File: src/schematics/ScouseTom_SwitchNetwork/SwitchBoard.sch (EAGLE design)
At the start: 87 parts, among them T1 PNP, U1 MCP73831, U10 ADG714BRUZ, U11 ADG714BRUZ, U12 ADUM1410ARWZ, U13 ADG714BRUZ, U14 ADG714BRUZ, U15 ADUM1412ARWZ, U2 ADG714BRUZ, U3 ADG714BRUZ, U4 TPS61090RSAR, U5 ADG714BRUZ, U6 ADG714BRUZ, U7 ADG714BRUZ, U8 LT1763CDE-5, U9 ADG714BRUZ, X1 USB-MICROB, X2 CTR_ARD, X3 CTR_OUT, X4 DSUB _T, X5 DSUB_B, X6 CTR_IN

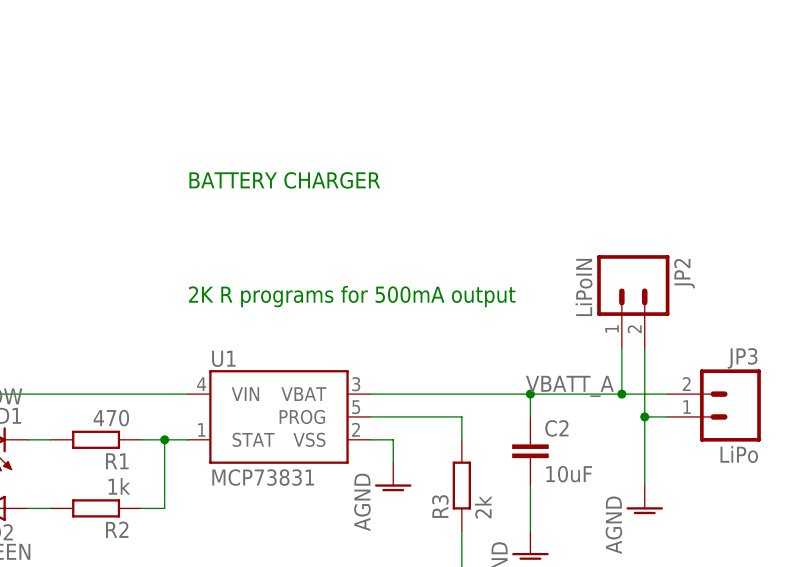
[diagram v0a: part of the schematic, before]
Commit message: Minor clarification in text in shcematic
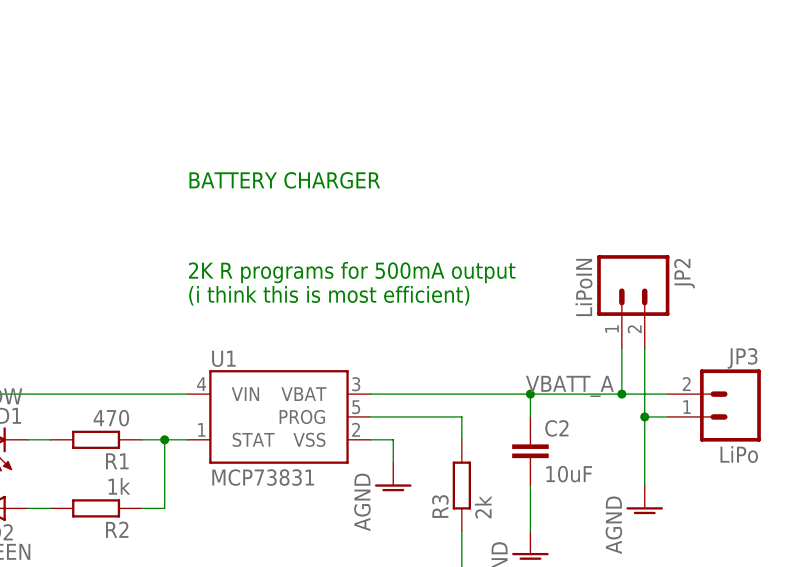
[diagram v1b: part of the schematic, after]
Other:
- note added: "2K R programs for 500mA output (i think this is most efficient)"
- note removed: "2K R programs for 500mA output"
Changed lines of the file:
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@@
 Split into free components</text>
 <text x="-246.38" y="208.28" size="1.778" layer="91">NOT CHANGED THIS YET</text>
-<text x="-490.22" y="203.2" size="1.778" layer="91">2K R programs for 500mA output</text>
+<text x="-490.22" y="203.2" size="1.778" layer="91">2K R programs for 500mA output
+(i think this is most efficient)</text>
 <text x="-416.56" y="220.98" size="1.778" layer="91">DISCONNECT BATTERY FROM REGULATORS TO TURN SHIT OFF</text>
 </plain>

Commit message: updated switchboard with proper daisy chain select and test 1 correct wiring
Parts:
- removed JP7: DCHN, pinhead:PINHD-2X9
- added U$1: PINHD-3X7GAP, pinhead:PINHD-3X7GAP
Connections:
- removed net GND_DCHN: JP7.4, X6.6
- removed net RESET_DCHN: JP7.14, X6.8
- removed net SYNC_DCHN: JP7.6, X6.4
- removed net TEST_1: JP7.15, R23.2, U15.VIC, X3.5
- removed net TEST_1_DCHN: JP7.16, X6.5
- new net DIN+_BRD: U$1.5, U12.VOB
- new net DIN-_BRD: U$1.7, U12.VOC
- new net SCLK_BRD: U$1.9, U12.VOD
- new net TEST_2_BRD: U$1.13, U15.VID
- new net VDD_BRD: C15.+, C18.1, C19.1, C24.1, C25.1, R23.2, U$1.1, U12.VDD2, U15.VDD2, U15.VIC, U8.OUT@1
- new net ~RESET_BRD: U$1.11, U15.VOA
- new net ~RESET_DCHN: U$1.12, X6.8
- new net ~SYNC_BRD: U$1.3, U12.VOA
- new net ~SYNC_DCHN: U$1.4, X6.4
- net AGND: now also X6.6; no longer JP7.3
- net DIN+: now also U$1.17; no longer JP7.7, U12.VOB
- net DIN+_DCHN: now also U$1.6; no longer JP7.8
- net DIN-: now also U$1.18; no longer JP7.9, U12.VOC
- net DIN-_DCHN: now also U$1.8; no longer JP7.10
- net SCLK: now also U$1.19; no longer JP7.11, U12.VOD
- net SCLK_DCHN: now also U$1.10; no longer JP7.12
- net TEST_2: now also U$1.21; no longer JP7.17, U15.VID
- net TEST_2_DCHN: now also U$1.14; no longer JP7.18
- net VDD: now also U$1.15, X3.5; no longer C15.+, C18.1, C19.1, C24.1, C25.1, JP7.1, U12.VDD2, U15.VDD2, U8.OUT@1
- net VDD_DCHN: now also U$1.2, X6.5; no longer JP7.2
- net ~RESET: now also U$1.20; no longer JP7.13, U15.VOA
- net ~SYNC: now also U$1.16; no longer JP7.5, U12.VOA

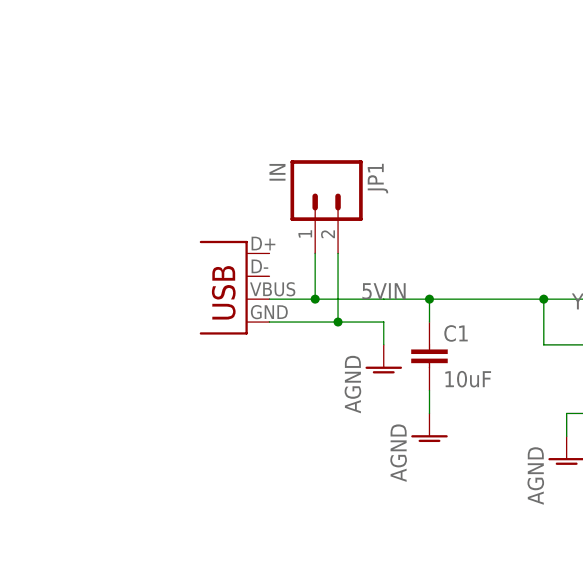
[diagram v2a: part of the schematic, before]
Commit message: Changed USB connector on SwitchBoard
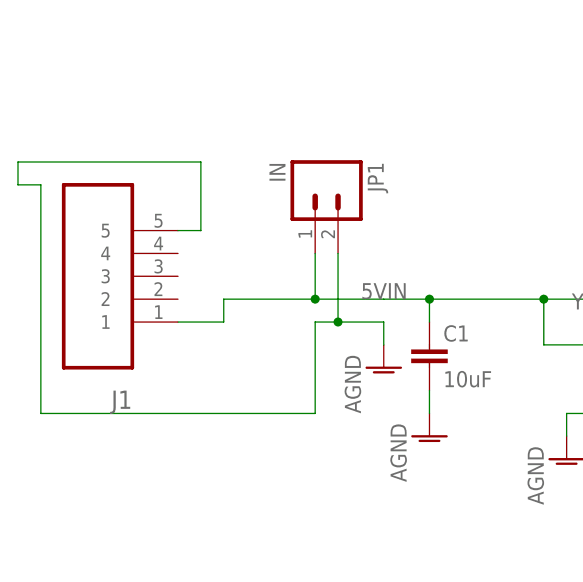
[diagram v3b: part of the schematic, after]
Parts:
- removed X1: USB-MICROB, SparkFun:USB-MICROB
- added J1: (no value), Molex-47346-0001:47346-0001
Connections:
- net 5VIN: now also J1.1; no longer X1.VBUS
- net AGND: now also J1.5; no longer X1.GND

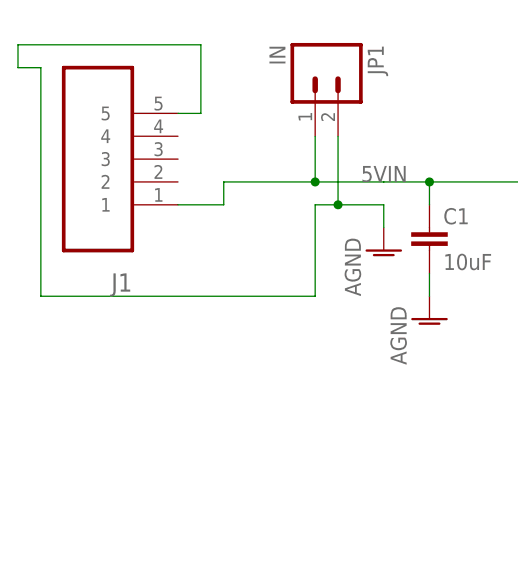
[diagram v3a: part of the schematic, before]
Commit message: Minor Silkscreen updates to SwitchBoard. New Gerber files and updated BOM and P&P with lipo connector
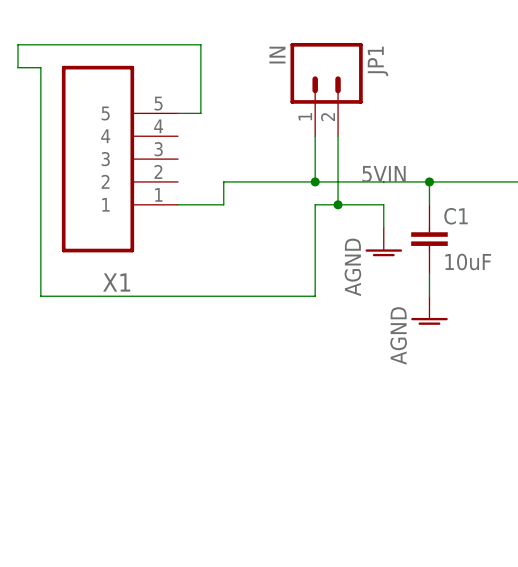
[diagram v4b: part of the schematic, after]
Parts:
- renumbered J1 to X1
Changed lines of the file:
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@@
 <part name="AGND51" library="supply1" deviceset="AGND" device=""/>
 <part name="U$1" library="pinhead" deviceset="PINHD-3X7GAP" device=""/>
-<part name="J1" library="Molex-47346-0001" deviceset="47346-0001" device=""/>
+<part name="X1" library="Molex-47346-0001" deviceset="47346-0001" device=""/>
 </parts>
 <sheets>
@@
 <instance part="AGND51" gate="VR1" x="248.92" y="121.92" rot="R90"/>
 <instance part="U$1" gate="G$1" x="383.54" y="114.3"/>
-<instance part="J1" gate="G$1" x="-571.5" y="195.58" rot="R180"/>
+<instance part="X1" gate="G$1" x="-571.5" y="195.58" rot="R180"/>
 </instances>
 <busses>
@@
 <pinref part="JP1" gate="G$1" pin="2"/>
 <pinref part="AGND1" gate="VR1" pin="AGND"/>
-<pinref part="J1" gate="G$1" pin="5"/>
+<pinref part="X1" gate="G$1" pin="5"/>
 <wire x1="-561.34" y1="200.66" x2="-558.8" y2="200.66" width="0.1524" layer="91"/>
 <wire x1="-558.8" y1="200.66" x2="-558.8" y2="208.28" width="0.1524" layer="91"/>
@@
 <wire x1="-556.26" y1="193.04" x2="-556.26" y2="190.5" width="0.1524" layer="91"/>
 <junction x="-546.1" y="193.04"/>
-<pinref part="J1" gate="G$1" pin="1"/>
+<pinref part="X1" gate="G$1" pin="1"/>
 <wire x1="-556.26" y1="190.5" x2="-561.34" y2="190.5" width="0.1524" layer="91"/>
 </segment>

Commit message: Updated Switchboard - pull down resistors, fixed routing, protection diodes and different battery connector
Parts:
- removed JP2: LiPoIN, SparkFun:M02PTH
- removed JP3: LiPo, SparkFun:M02-JST-2MM-SMT
- added D1, D2: 1N4148W-7-F, diode:DIODE-SOD123
- added R25, R26, R27, R28, R29, R30, R31, R32, R33, R34, R35, R36, R37, R38: 10k, rcl:R-EU_R0402
- added TP1, TP2: TPPAD1-20, testpad:TPPAD1-20
- added X7: JST-XH-02-PIN-LONG-PAD, Rembrandt Electronics - JST XH Connectors v1-0:JST-XH-02-PIN-LONG-PAD
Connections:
- net N$12 renamed CTR_IN_SHLD
- net 5VIN: now also D1.C
- net AGND: now also D1.A, D2.A, R30.1, R33.1, R34.1, R35.1, R36.1, R37.1, R38.1, X7-1.S; no longer JP2.2, JP3.1
- net DIN+_DCHN: now also R36.2
- net DIN+_IN: now also R29.2
- net DIN-_DCHN: now also R37.2
- net DIN-_IN: now also R32.2
- net GND: now also R25.2, R26.2, R27.1, R28.1, R29.1, R31.1, R32.1
- net IN+: now also TP1.TP
- net IN-: now also TP2.TP
- net RESET_IN: now also R31.2
- net SCLK_DCHN: now also R35.2
- net SCLK_IN: now also R26.1
- net SYNC_IN: now also R28.2
- net TEST_1_IN: now also R27.2
- net TEST_2_DCHN: now also R34.2
- net TEST_2_IN: now also R25.1
- net VBATT_A: now also D2.C, X7-2.S; no longer JP2.1, JP3.2
- net VDD_DCHN: now also R30.2
- net ~RESET_DCHN: now also R38.2
- net ~SYNC_DCHN: now also R33.2
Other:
- note added: "DAISY CHAIN SELECTOR"
